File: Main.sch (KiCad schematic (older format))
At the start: 7 parts

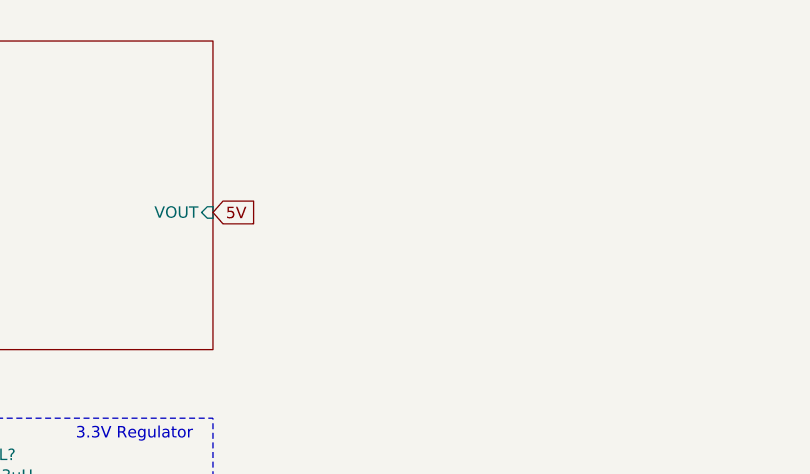
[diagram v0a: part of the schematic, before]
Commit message: moved solar cell current sensor and load switch to root sheet
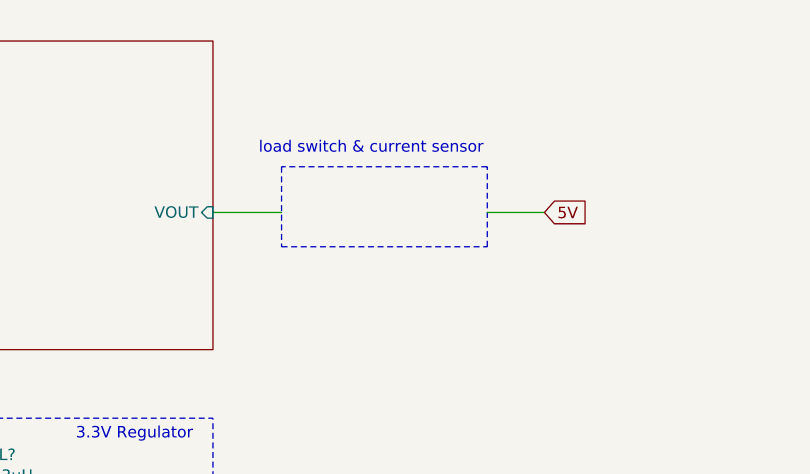
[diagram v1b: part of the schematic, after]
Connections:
- wire segments 11 -> 13
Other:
- note added: "load switch & current sensor"
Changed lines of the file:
@@
 EESchema Schematic File Version 4
+LIBS:Main-cache
 EELAYER 29 0
 EELAYER END
@@
 F2 "VOUT" I R 4050 5600 50
 $EndSheet
-Text GLabel 4050 5600 2    50   Input ~ 0
+Text GLabel 5500 5600 2    50   Input ~ 0
 5V
 $Comp
@@
 	1    0    0    -1
 $EndComp
+Wire Wire Line
+	4050 5600 4350 5600
+Wire Wire Line
+	5500 5600 5250 5600
+Wire Notes Line
+	4350 5400 4350 5750
+Wire Notes Line
+	4350 5750 5250 5750
+Wire Notes Line
+	5250 5750 5250 5400
+Wire Notes Line
+	5250 5400 4350 5400
+Text Notes 4250 5350 0    50   ~ 0
+load switch & current sensor
 $EndSCHEMATC

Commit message: added schematic for Batt, BCR, and PDU
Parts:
- added BT?: Cell1, symbol Device:Battery_Cell
- added BT?: Cell2, symbol Device:Battery_Cell
- added C?: 22u, symbol Device:C
- added C?: 0.47u, symbol Device:C
- added C?: 10u, symbol Device:C
- added C? (x5): 0.1u, symbol Device:C
- added C? (x4): 150u, symbol Device:C
- added D?: D_Schottky, symbol Device:D_Schottky
- added J?: USB_A MALE, symbol Connector_Generic:Conn_01x02
- added J?: USB_A FEMALE, symbol Connector:USB_A
- added L?: 6.8u, symbol Device:L
- added PS?: HS-40012, Converter_ACDC:Converter_ACDC_Hahn_HS-400xx_THT, symbol Converter_ACDC:HS-40012
- added Q?: Q_PMOS_SDG, symbol Device:Q_PMOS_SDG
- added R?: 68m, symbol Device:R
- added R?: 2.2k, symbol Device:R
- added R? (x4): R, symbol Device:R
- added TH?: 10k, symbol Device:Thermistor_NTC
- added U? (x4): TPS2557, symbol CustomSymbols:TPS2557
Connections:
- net labels added: +3.3V, +5V, ACS, BAT, CHRG, NTC, OBC, PAYLOAD, RF
- net labels removed: 3.3V, 5V
- wire segments 13 -> 71
- no-connect marks 1 -> 11
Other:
- note added: "2-cell 1S2P Li-Ion Battery Pack"
- note added: "Battery Charge Regulator (BCR)"
- note added: "External Charging Circuit\n"
- note added: "Ground Leg Inhibit"
- note added: "Power Distribution Unit (PDU)"
- moved on the sheet: C?, L?, R?, U?

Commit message: added current sensing circuit and 5v/3.3v voltage monitoring
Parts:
- added R? (x5): TBD, symbol Device:R_Shunt
- added R?: 250k, symbol Device:R_Shunt
- added R?: 250k, symbol Device:R
- added R?: 165k, symbol Device:R_Shunt
- added R?: 165k, symbol Device:R
- U?: symbol MSP430:MSP430F5529IPN -> Main-rescue:MSP430F5529IPN-MSP430
- U? (x4): symbol CustomSymbols:TPS2557 -> Main-rescue:TPS2557-CustomSymbols
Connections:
- net labels added: 3.3V_ADC, 5V_ADC, ACS+, ACS-, EPS+, EPS-, Ibat+, Ibat-, Ipv+, Ipv-, OBC+, OBC-, PAYLOAD+, PAYLOAD-, RF+, RF-
- wire segments 71 -> 136
- no-connect marks 11 -> 13

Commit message: Imported 5V Regulator and 30 minute timer
Added libraries to the working libraries in the main project. Also imported the 4.2-5VDC regulator and 30 minute timer schematics.
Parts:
- added C?: 0.01uF, symbol 555_timer-rescue:0.01uF
- added C?: 180uF, symbol 555_timer-rescue:180uF
- added C?: C1uF, symbol 4.2-5V_regulator:C1uF
- added C? (x4): C22uF, symbol 4.2-5V_regulator:C22uF
- added D? (x2): FET(reversed), symbol 555_timer-rescue:FET(reversed)
- added D?: Diode, symbol 555_timer-rescue:Diode
- added L?: L1.5uH, symbol 4.2-5V_regulator:L1.5uH
- added R? (x2): 10k, symbol 555_timer-rescue:10k
- added R?: 10M, symbol 555_timer-rescue:10M
- added R?: R150K, symbol 4.2-5V_regulator:R150K
- added R?: R787K, symbol 4.2-5V_regulator:R787K
- added U?: LM555_TIMER, symbol 555_timer-rescue:LM555_TIMER
- added U?: MP3423, symbol 4.2-5V_regulator:MP3423
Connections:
- net labels added: Coin_cell, GND, GNDA, IN, MCU_CTRL, OUT, Sw, Trig
- wire segments 136 -> 197
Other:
- note added: "30 Minute Timer"
- note added: "4.2 - 5VDC Regulator"
- note added: "A\n"
- note added: "April 6/2018"
- note added: "DAL ORBITS 30 minute inhibit switch"
- note added: "Power"
- note added: "System Switch"
- note added: "Zach McQuaid"
- moved on the sheet: C?, L?, R?, U?

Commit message: changed msp430
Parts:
- C?: symbol 555_timer-rescue:0.01uF -> Main-rescue:0.01uF-555_timer-rescue
- C?: symbol 555_timer-rescue:180uF -> Main-rescue:180uF-555_timer-rescue
- D? (x2): symbol 555_timer-rescue:FET(reversed) -> Main-rescue:FET(reversed)-555_timer-rescue
- D?: symbol 555_timer-rescue:Diode -> Main-rescue:Diode-555_timer-rescue
- R? (x2): symbol 555_timer-rescue:10k -> Main-rescue:10k-555_timer-rescue
- R?: symbol 555_timer-rescue:10M -> Main-rescue:10M-555_timer-rescue
- U?: symbol 555_timer-rescue:LM555_TIMER -> Main-rescue:LM555_TIMER-555_timer-rescue
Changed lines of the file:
@@
 EESchema Schematic File Version 4
 LIBS:Main-cache
-LIBS:4.2-5V_regulator-cache
-LIBS:555_timer-cache
 EELAYER 29 0
 EELAYER END
 $Descr A2 23386 16535
 encoding utf-8
-Sheet 1 29
+Sheet 1 28
 Title "Electrical Power System"
 Date "2019-04-25"
 Rev "1.0"
 Comp "Dalhousie Space Systems"
-Comment1 ""
+Comment1 "mark.crispo@dal.ca"
 Comment2 ""
 Comment3 ""
@@
 	12200 13200 12200 13250
 $Comp
-L 555_timer-rescue:GNDA #PWR?
+L Main-rescue:GNDA-555_timer-rescue #PWR?
 U 1 1 5CA9BD0E
 P 11450 11700
@@
 $EndComp
 $Comp
-L 555_timer-rescue:GNDA #PWR?
+L Main-rescue:GNDA-555_timer-rescue #PWR?
 U 1 1 5CA9BCDC
 P 12200 13250
@@
 Connection ~ 9300 12050
 $Comp
-L 555_timer-rescue:10k R?
+L Main-rescue:10k-555_timer-rescue R?
 U 1 1 5CA9B9BF
 P 9300 11550
@@
 	13150 12450 13500 12450
 $Comp
-L 555_timer-rescue:180uF C?
+L Main-rescue:180uF-555_timer-rescue C?
 U 1 1 5CA9B645
 P 13850 12850
@@
 $EndComp
 $Comp
-L 555_timer-rescue:10M R?
+L Main-rescue:10M-555_timer-rescue R?
 U 1 1 5CA9B579
 P 13850 11600
@@
 $EndComp
 $Comp
-L 555_timer-rescue:Diode D?
+L Main-rescue:Diode-555_timer-rescue D?
 U 1 1 5CA9B4AA
 P 14250 11700
@@
 $EndComp
 $Comp
-L 555_timer-rescue:0.01uF C?
+L Main-rescue:0.01uF-555_timer-rescue C?
 U 1 1 5CA9B433
 P 13500 12850
@@
 $EndComp
 $Comp
-L 555_timer-rescue:FET(reversed) D?
+L Main-rescue:FET(reversed)-555_timer-rescue D?
 U 1 1 5CA9B390
 P 8800 12050
@@
 $EndComp
 $Comp
-L 555_timer-rescue:FET(reversed) D?
+L Main-rescue:FET(reversed)-555_timer-rescue D?
 U 1 1 5CA9B2ED
 P 9400 12450
@@
 $EndComp
 $Comp
-L 555_timer-rescue:10k R?
+L Main-rescue:10k-555_timer-rescue R?
 U 1 1 5CA9B240
 P 9900 12850
@@
 $EndComp
 $Comp
-L 555_timer-rescue:LM555_TIMER U?
+L Main-rescue:LM555_TIMER-555_timer-rescue U?
 U 1 1 5CA9B022
 P 12250 12050

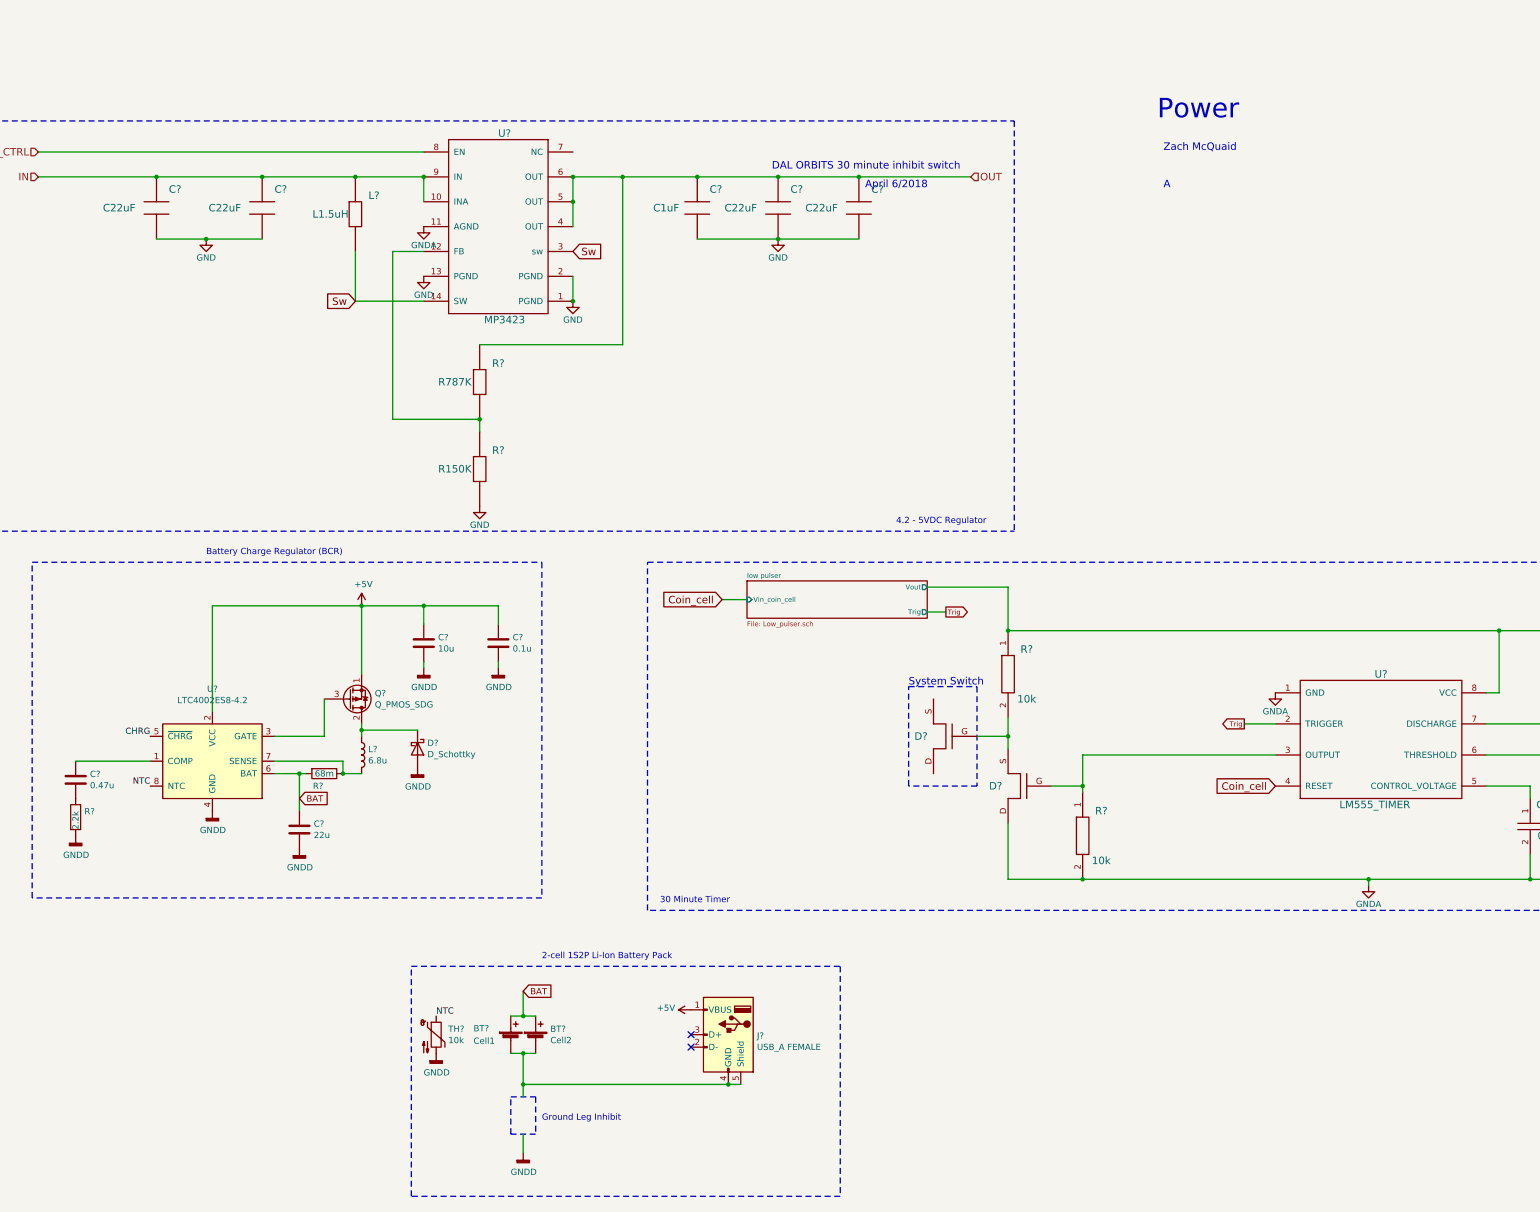
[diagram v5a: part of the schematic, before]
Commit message: Added two more batteries for 4P configuration, added TI BQ297xx battery protection IC and PTC resettable fuse
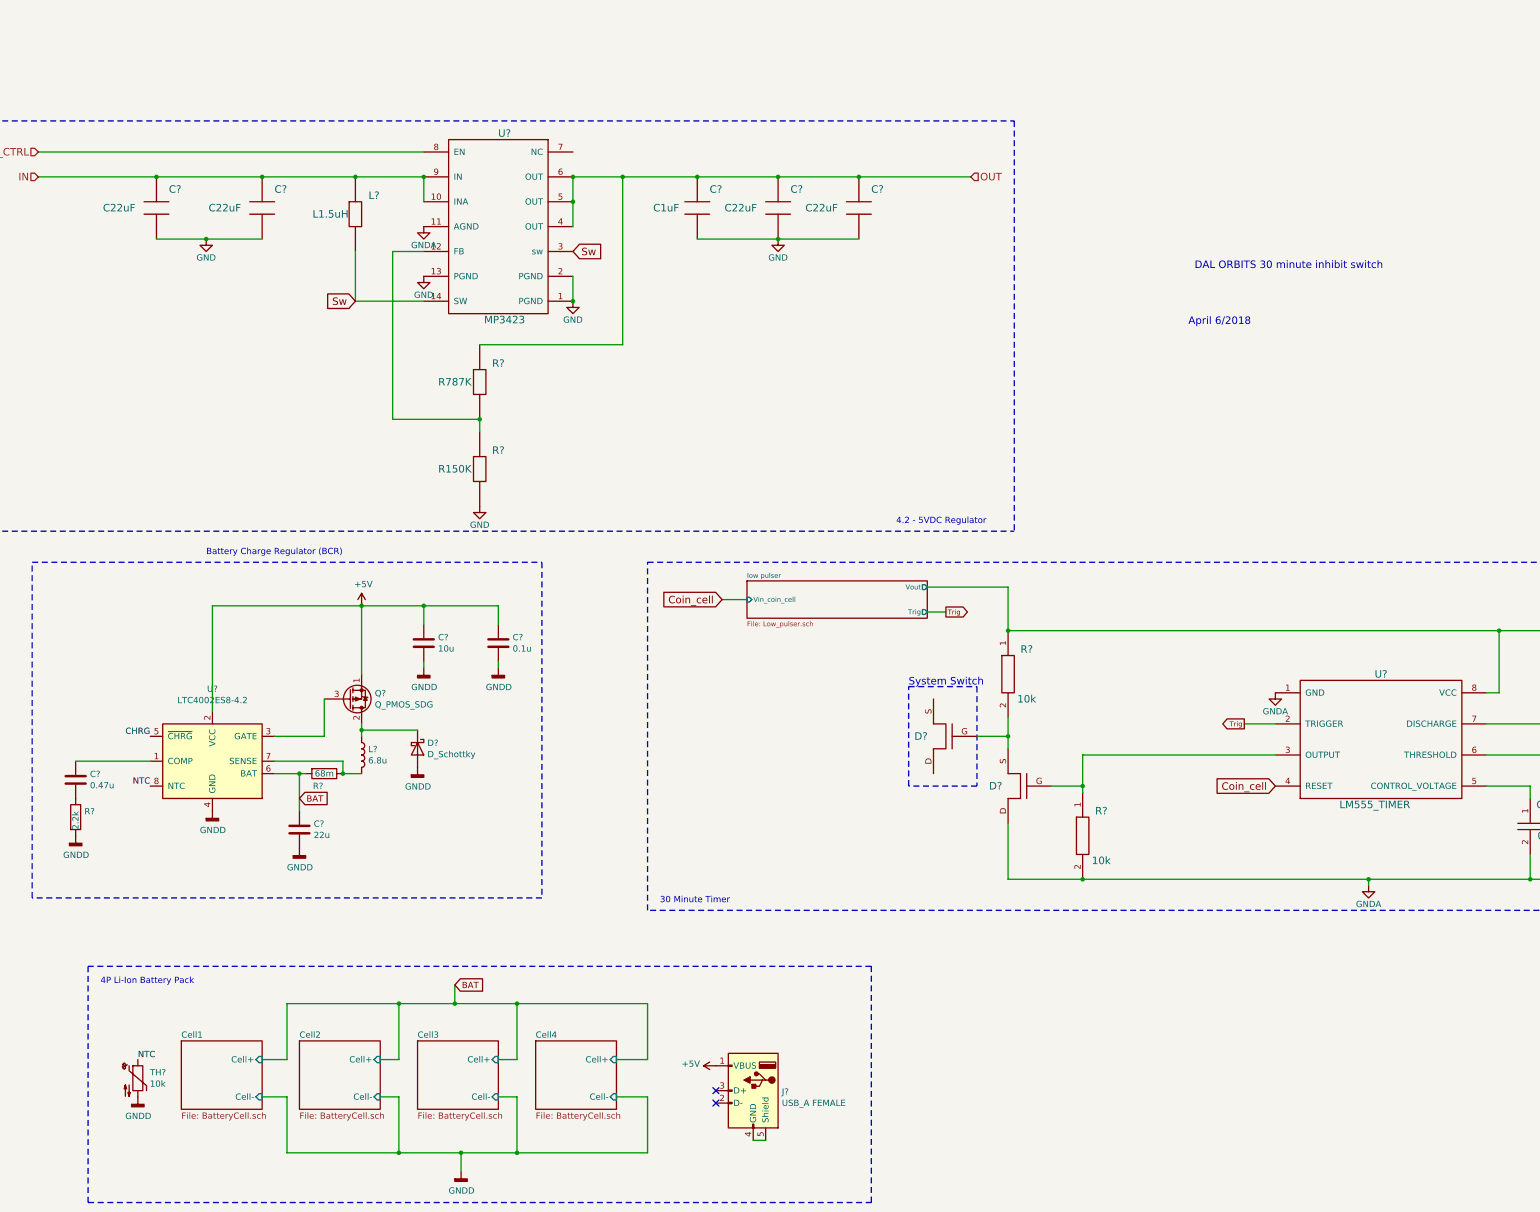
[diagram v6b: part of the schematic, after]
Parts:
- removed BT?: Cell1, symbol Device:Battery_Cell
- removed BT?: Cell2, symbol Device:Battery_Cell
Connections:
- wire segments 197 -> 214
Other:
- note added: "4P Li-Ion Battery Pack"
- note removed: "2-cell 1S2P Li-Ion Battery Pack"
- note removed: "A\n"
- note removed: "Ground Leg Inhibit"
- note removed: "Power"
- note removed: "Zach McQuaid"
- moved on the sheet: J?, TH?
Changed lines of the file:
@@
 $Descr A2 23386 16535
 encoding utf-8
-Sheet 1 28
+Sheet 1 32
 Title "Electrical Power System"
 Date "2019-04-25"
@@
 L Device:Thermistor_NTC TH?
 U 1 1 5CB7A5F8
-P 4700 14450
-F 0 "TH?" H 4797 14496 50  0000 L CNN
-F 1 "10k" H 4797 14405 50  0000 L CNN
-F 2 "" H 4700 14500 50  0001 C CNN
-F 3 "~" H 4700 14500 50  0001 C CNN
-	1    4700 14450
+P 2300 14800
+F 0 "TH?" H 2397 14846 50  0000 L CNN
+F 1 "10k" H 2397 14755 50  0000 L CNN
+F 2 "" H 2300 14850 50  0001 C CNN
+F 3 "~" H 2300 14850 50  0001 C CNN
+	1    2300 14800
 	1    0    0    -1
 $EndComp
@@
 Wire Wire Line
 	4600 11500 4600 11450
-NoConn ~ 6750 14450
-NoConn ~ 6750 14550
+NoConn ~ 6950 14900
+NoConn ~ 6950 15000
 $Comp
 L Connector_Generic:Conn_01x02 J?
@@
 	1    0    0    -1
 $EndComp
-$Comp
-L Device:Battery_Cell BT?
-U 1 1 5CC9EF70
-P 5300 14500
-F 0 "BT?" H 5000 14600 50  0000 L CNN
-F 1 "Cell1" H 5000 14500 50  0000 L CNN
-F 2 "" V 5300 14560 50  0001 C CNN
-F 3 "~" V 5300 14560 50  0001 C CNN
-	1    5300 14500
-	1    0    0    -1
-$EndComp
-$Comp
-L Device:Battery_Cell BT?
-U 1 1 5CC9FB6D
-P 5500 14500
-F 0 "BT?" H 5618 14596 50  0000 L CNN
-F 1 "Cell2" H 5618 14505 50  0000 L CNN
-F 2 "" V 5500 14560 50  0001 C CNN
-F 3 "~" V 5500 14560 50  0001 C CNN
-	1    5500 14500
-	1    0    0    -1
-$EndComp
-Wire Wire Line
-	5500 14300 5400 14300
-$Comp
-L Connector:USB_A J?
-U 1 1 5CB82268
-P 7050 14450
-F 0 "J?" H 6820 14441 50  0000 R CNN
-F 1 "USB_A FEMALE" H 6820 14350 50  0000 R CNN
-F 2 "" H 7200 14400 50  0001 C CNN
-F 3 " ~" H 7200 14400 50  0001 C CNN
-	1    7050 14450
-	-1   0    0    -1
-$EndComp
-Wire Notes Line
-	5300 14950 5500 14950
-Wire Notes Line
-	5500 14950 5500 15250
-Wire Notes Line
-	5500 15250 5300 15250
-Wire Notes Line
-	5300 15250 5300 14950
-Text Notes 5550 15150 0    50   ~ 0
-Ground Leg Inhibit
-Wire Wire Line
-	5400 15250 5400 15400
+Wire Wire Line
+	4900 15400 4900 15550
 $Comp
 L power:GNDD #PWR?
 U 1 1 5CCACD90
-P 5400 15400
-F 0 "#PWR?" H 5400 15150 50  0001 C CNN
-F 1 "GNDD" H 5404 15245 50  0000 C CNN
-F 2 "" H 5400 15400 50  0001 C CNN
-F 3 "" H 5400 15400 50  0001 C CNN
-	1    5400 15400
-	1    0    0    -1
-$EndComp
-Wire Wire Line
-	5400 14300 5400 14100
-Connection ~ 5400 14300
-Wire Wire Line
-	5400 14300 5300 14300
-Text GLabel 5400 14100 2    50   Input ~ 0
-BAT
-Wire Wire Line
-	5300 14600 5400 14600
-Wire Wire Line
-	5400 14600 5400 14850
-Connection ~ 5400 14600
-Wire Wire Line
-	5400 14600 5500 14600
-Wire Wire Line
-	7050 14850 7150 14850
-Wire Wire Line
-	7050 14850 5400 14850
-Connection ~ 7050 14850
-Connection ~ 5400 14850
-Wire Wire Line
-	5400 14850 5400 14950
+P 4900 15550
+F 0 "#PWR?" H 4900 15300 50  0001 C CNN
+F 1 "GNDD" H 4904 15395 50  0000 C CNN
+F 2 "" H 4900 15550 50  0001 C CNN
+F 3 "" H 4900 15550 50  0001 C CNN
+	1    4900 15550
+	1    0    0    -1
+$EndComp
+Wire Wire Line
+	7250 15300 7350 15300
 $Comp
 L power:+5V #PWR?
 U 1 1 5CCB63EF
-P 6750 14250
-F 0 "#PWR?" H 6750 14100 50  0001 C CNN
-F 1 "+5V" V 6765 14378 50  0000 L CNN
-F 2 "" H 6750 14250 50  0001 C CNN
-F 3 "" H 6750 14250 50  0001 C CNN
-	1    6750 14250
+P 6950 14700
+F 0 "#PWR?" H 6950 14550 50  0001 C CNN
+F 1 "+5V" V 6965 14828 50  0000 L CNN
+F 2 "" H 6950 14700 50  0001 C CNN
+F 3 "" H 6950 14700 50  0001 C CNN
+	1    6950 14700
 	0    -1   -1   0
 $EndComp
@@
 Text GLabel 3600 12550 2    50   Input ~ 0
 BAT
-Text Label 4700 14300 0    50   ~ 0
+Text Label 2300 14650 0    50   ~ 0
 NTC
 $Comp
 L power:GNDD #PWR?
 U 1 1 5CCBA53E
-P 4700 14600
-F 0 "#PWR?" H 4700 14350 50  0001 C CNN
-F 1 "GNDD" H 4704 14445 50  0000 C CNN
-F 2 "" H 4700 14600 50  0001 C CNN
-F 3 "" H 4700 14600 50  0001 C CNN
-	1    4700 14600
+P 2300 14950
+F 0 "#PWR?" H 2300 14700 50  0001 C CNN
+F 1 "GNDD" H 2304 14795 50  0000 C CNN
+F 2 "" H 2300 14950 50  0001 C CNN
+F 3 "" H 2300 14950 50  0001 C CNN
+	1    2300 14950
 	1    0    0    -1
 $EndComp
@@
 Text Notes 2850 10600 0    50   ~ 0
 Battery Charge Regulator (BCR)
-Wire Notes Line
-	4500 13900 7950 13900
-Wire Notes Line
-	7950 13900 7950 15750
-Wire Notes Line
-	7950 15750 4500 15750
-Wire Notes Line
-	4500 15750 4500 13900
-Text Notes 5550 13850 0    50   ~ 0
-2-cell 1S2P Li-Ion Battery Pack
+Text Notes 2000 14050 0    50   ~ 0
+4P Li-Ion Battery Pack
 $Comp
 L power:+5V #PWR?
@@
 Text Notes 8400 10350 0    50   ~ 0
 4.2 - 5VDC Regulator
-Text Notes 7400 7500 0    60   ~ 0
+Text Notes 10800 8300 0    60   ~ 0
 DAL ORBITS 30 minute inhibit switch
-Text Notes 10550 7650 0    60   ~ 0
-A\n
-Text Notes 8150 7650 0    60   ~ 0
+Text Notes 10750 8750 0    60   ~ 0
 April 6/2018
-Text Notes 10550 7350 0    60   ~ 0
-Zach McQuaid
-Text Notes 10500 7100 0    157  ~ 0
-Power
 Connection ~ 9900 12450
 Wire Wire Line
@@
 Text Notes 6500 13400 0    50   ~ 0
 30 Minute Timer
+$Sheet
+S 2650 14500 650  550
+U 5D07F3FC
+F0 "Cell1" 50
+F1 "BatteryCell.sch" 50
+F2 "Cell+" I R 3300 14650 50
+F3 "Cell-" I R 3300 14950 50
+$EndSheet
+$Sheet
+S 3600 14500 650  550
+U 5D0A75A0
+F0 "Cell2" 50
+F1 "BatteryCell.sch" 50
+F2 "Cell+" I R 4250 14650 50
+F3 "Cell-" I R 4250 14950 50
+$EndSheet
+$Sheet
+S 4550 14500 650  550
+U 5D0B1FBC
+F0 "Cell3" 50
+F1 "BatteryCell.sch" 50
+F2 "Cell+" I R 5200 14650 50
+F3 "Cell-" I R 5200 14950 50
+$EndSheet
+$Sheet
+S 5500 14500 650  550
+U 5D0BC9BA
+F0 "Cell4" 50
+F1 "BatteryCell.sch" 50
+F2 "Cell+" I R 6150 14650 50
+F3 "Cell-" I R 6150 14950 50
+$EndSheet
+Wire Wire Line
+	3300 14650 3500 14650
+Wire Wire Line
+	3500 14650 3500 14200
+Wire Wire Line
+	3500 14200 4400 14200
+Wire Wire Line
+	6400 14200 6400 14650
+Wire Wire Line
+	6150 14650 6400 14650
+Wire Wire Line
+	5200 14650 5350 14650
+Wire Wire Line
+	5350 14650 5350 14200
+Connection ~ 5350 14200
+Wire Wire Line
+	5350 14200 6400 14200
+Wire Wire Line
+	4250 14650 4400 14650
+Wire Wire Line
+	4400 14650 4400 14200
+Connection ~ 4400 14200
+Wire Wire Line
+	4400 14200 4850 14200
+Wire Wire Line
+	3300 14950 3500 14950
+Wire Wire Line
+	3500 14950 3500 15400
+Wire Wire Line
+	3500 15400 4400 15400
+Wire Wire Line
+	6400 15400 6400 14950
+Wire Wire Line
+	6400 14950 6150 14950
+Wire Wire Line
+	5200 14950 5350 14950
+Wire Wire Line
+	5350 14950 5350 15400
+Connection ~ 5350 15400
+Wire Wire Line
+	5350 15400 6400 15400
+Wire Wire Line
+	4250 14950 4400 14950
+Wire Wire Line
+	4400 14950 4400 15400
+Connection ~ 4400 15400
+Wire Wire Line
+	4400 15400 4900 15400
+Connection ~ 4900 15400
+Wire Wire Line
+	4900 15400 5350 15400
+Wire Wire Line
+	4850 14200 4850 14050
+Connection ~ 4850 14200
+Wire Wire Line
+	4850 14200 5350 14200
+Text GLabel 4850 14050 2    50   Input ~ 0
+BAT
+$Comp
+L Connector:USB_A J?
+U 1 1 5CB82268
+P 7250 14900
+F 0 "J?" H 7020 14891 50  0000 R CNN
+F 1 "USB_A FEMALE" H 7020 14800 50  0000 R CNN
+F 2 "" H 7400 14850 50  0001 C CNN
+F 3 " ~" H 7400 14850 50  0001 C CNN
+	1    7250 14900
+	-1   0    0    -1
+$EndComp
+Wire Notes Line
+	1900 15800 8200 15800
+Wire Notes Line
+	8200 15800 8200 13900
+Wire Notes Line
+	8200 13900 1900 13900
+Wire Notes Line
+	1900 13900 1900 15800
 $EndSCHEMATC
